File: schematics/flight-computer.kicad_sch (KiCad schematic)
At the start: 45 parts, among them J1 BATT, J2 SERIAL, J3 BLACKBOX, P1 SWD_TC, P2 GPS, P3 TLM, U1 MAX604, U10 MAX14787E, U11 MAX14787E, U12 NC7SZ04, U2 MAX604, U3 STM32F405RGT6, U9 CDCLVC1103PW, Y1 LFTCXO068373

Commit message: Complete revision 1 schematic
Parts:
- removed C1: 100n, Strix:C_0402, symbol Strix:C
- removed C2, C3, C5, C6: 10u, Strix:C_0402, symbol Strix:C
- removed C31: 10n, Strix:C_0402, symbol Strix:C
- removed C4: 1n, Strix:C_0402, symbol Strix:C
- removed J2: SERIAL, Strix:Molex_Nano-Fit_105314-1106, symbol Strix:Conn_01x06
- removed P1: SWD_TC, Strix:SWD_TC, symbol Strix:SWD_TC
- removed R1: 200k, Strix:R_0402, symbol Strix:R
- removed R10: 10, Strix:R_0402, symbol Strix:R
- removed R5: 120, Strix:R_0402, symbol Strix:R
- removed R8, R9: 510k, Strix:R_0402, symbol Strix:R
- removed U1, U2: MAX604, Strix:MAX604, symbol Strix:MAX604
- removed U10: MAX14787E, Strix:MAX14787E, symbol Strix:MAX14787E
- removed U12: NC7SZ04, cusf:SOT-23-5, symbol Strix:NC7SZ04
- removed U9: CDCLVC1103PW, Strix:CDCLVC1103PW, symbol Strix:CDCLVC1103PW
- removed Y1: LFTCXO068373, Strix:LFTCXO068373, symbol Strix:LFTCXO068373
- added D1, D10, D11, D2, D3, D4, D5, D6, D7, D8, D9: ESD_DIODE, cusf:D_0402, symbol Strix:ESD_DIODE
- added J1: SWD, symbol Strix:Conn_02x05
- added J3: CHG, symbol Strix:Conn_01x02
- added J4: USB MICRO B, symbol Strix:Conn_01x05
- R2: value 10 -> 10k; footprint Strix:R_0402 -> (none)
- R3: value 100k -> 10k; footprint Strix:R_0402 -> (none)
- renumbered C7 to C1, C16 to C10, C8 to C2, C9 to C3, C10 to C4, C11 to C5, C12 to C6, C13 to C7, C14 to C8, C15 to C9, D1 to D12, D2 to D13, J1 to J2, J3 to J5, P2 to P1, P3 to P2, R6 to R1, U3 to U1, U11 to U2
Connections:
- net RADIO_CLK is gone; now on net USB_FS_VBUS: R2.2
- net USART1_TX is gone; now on net USB_FS_VBUS: U1.42 (PA9)
- net 3v3: now also D4.2, J1.1 (Pin_1)
- net GND: now also R2.1, D10.1, D11.1, D4.1, D5.1, D6.1, D7.1, D8.1, D9.1, J1.3 (Pin_3), J1.5 (Pin_5), J1.9 (Pin_9), J4.5 (Pin_5); no longer J2.3 (Pin_3)
- net SWDIO: now also J1.2 (Pin_2)
- net UART4_RX+: now also D5.2
- net UART4_RX-: now also D7.2
- net UART4_TX+: now also D9.2
- net UART4_TX-: now also D11.2
- net USB_FS_VBUS: now reaches R3.1
- net USB_FS_D+: now reaches U1.44 (PA11)
- net USB_FS_D+: now also D10.2, J4.3 (Pin_3)
- net USB_FS_D-: now reaches U1.45 (PA12)
- net USB_FS_D-: now also D8.2, J4.2 (Pin_2)
- net CHG_SDN: now reaches U1.50 (PA15)
- net IMU_PR_CL: now reaches U1.58 (PB6)
- net IMU_PR_DA: now reaches U1.59 (PB7)
- net 1v8: no longer names the net of R3.2
- net 1v8: now also D6.2, J4.1 (Pin_1)
- net BATT_MON renamed PSU/BATT_MON
- net PSU/BATT_MON: now also D1.1
- net MCU_CLK: no longer names the net of U1.5 (PH0)
- net USART1_RX: no longer names the net of U1.43 (PA10)
- net VBATT renamed PSU/BATT+
- net PSU/BATT+: now also D3.1
- net ~{RST} renamed NRST
- net NRST: now also J1.10 (Pin_10)
- new net PSU/BATT-: D1.2, D3.2, J2.3 (Pin_3)
- new net PSU/CHG+: D2.1, J3.1 (Pin_1)
- new net PSU/CHG-: D2.2, J3.2 (Pin_2)
- new net SWCLK: J1.4 (Pin_4)
- new net SWO: J1.6 (Pin_6)
- no-connect marks 28 -> 24
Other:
- added sheet PSU (psu.kicad_sch)
- sheet Altimeter ports: added IMU_PR_CL, IMU_PR_DA; removed none
- sheet Radio ports: added none; removed RADIO_CLK
- note added: "8.9 - 22V DC Charger Input"
- note added: "Blackbox Serial (RS-485)"
- note added: "SWD"
- note added: "USB Serial Out"
- note removed: "1v8 Power (300mA Max)"
- note removed: "26MHz Oscillator"
- note removed: "3v3 Power (300mA Max)"
- note removed: "Clipped Sine -> LVCMOS"
- note removed: "Clock Buffer"
- note removed: "Clock Distribution"
- note removed: "Note: - 3-output IC used because 2-output version not in stock - RADIO_CLK line should be properly impedance matched (currently not) - Clock buffer requires ferrite bead (see datasheet) - Coupling cap on output of TCXO should be < 1n"
- note removed: "Programming Interface (SWD)"
- note removed: "Serial Out (RS-485)"
- note removed: "To Blackbox (RS-485)"
- note removed: "USART1 <-> RS-422"
- moved on the sheet: C1, C10, C2, C3, C4, C5, C6, C7, C8, C9, D12, D13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

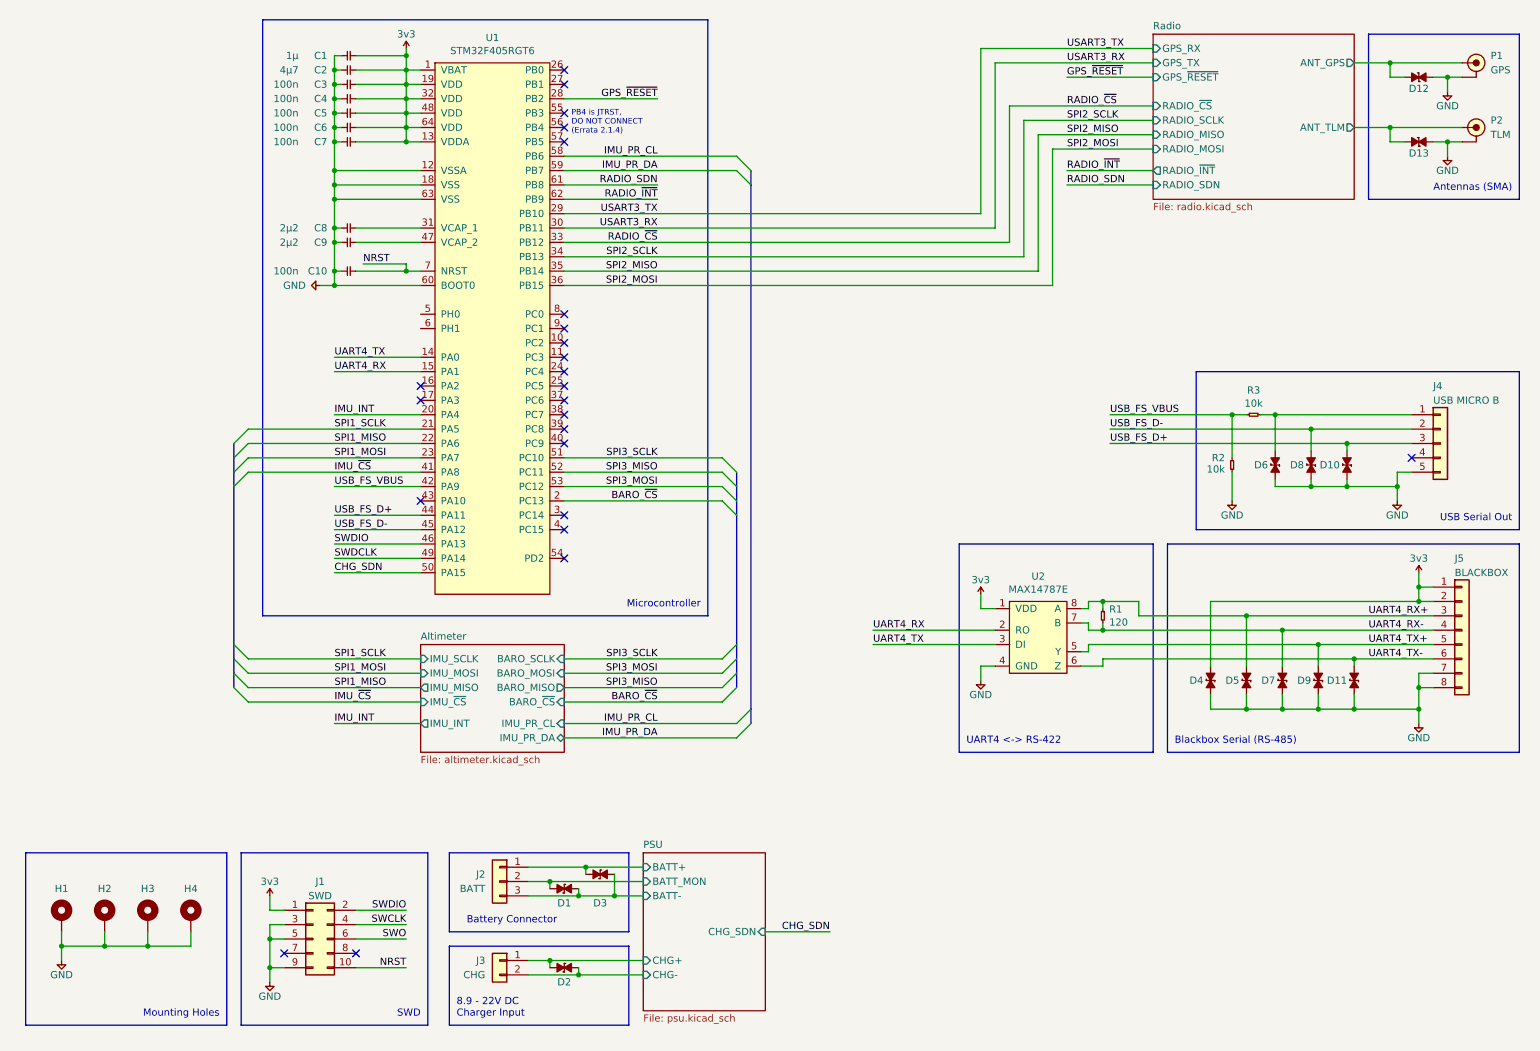
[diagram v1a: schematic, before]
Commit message: Add oscillators and clean up schematics
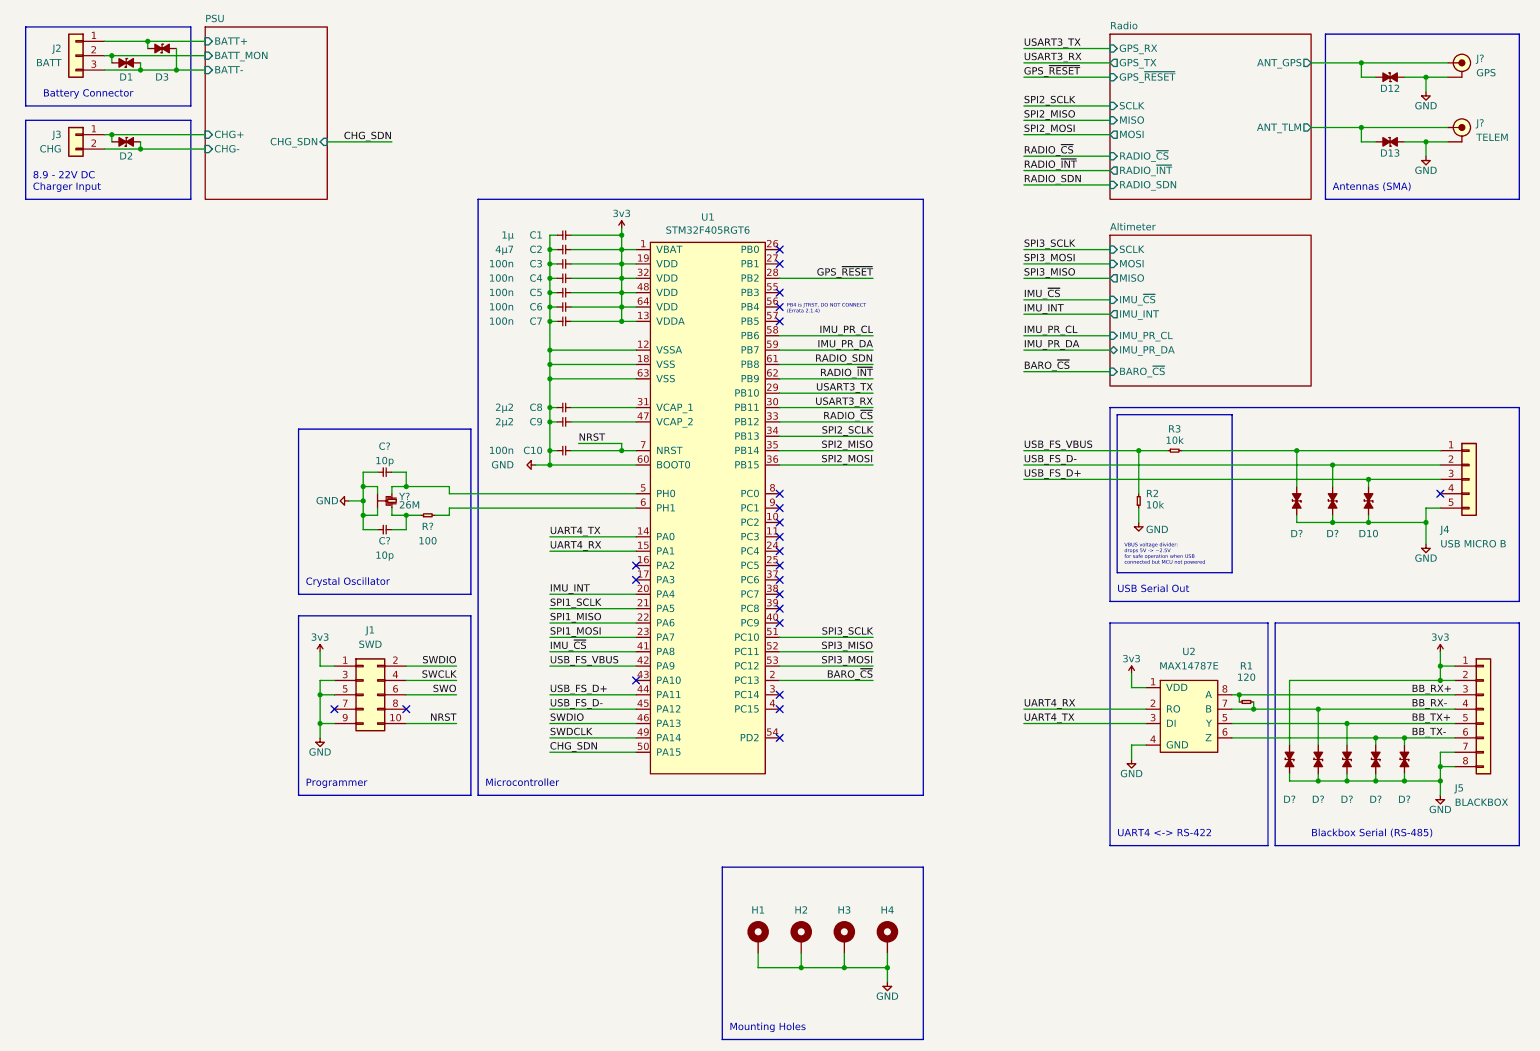
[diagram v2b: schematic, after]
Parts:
- removed D11, D4, D5, D6, D7, D8, D9: ESD_DIODE, cusf:D_0402, symbol Strix:ESD_DIODE
- removed P1: GPS, Strix:SMA-EDGE, symbol Strix:COAX
- removed P2: TLM, Strix:SMA-EDGE, symbol Strix:COAX
- added C? (x2): 10p, Strix:C_0402, symbol Strix:C
- added D? (x7): D_ESD, Strix:D_0402, symbol Strix:D_ESD
- added J?: GPS, Strix:SMA-EDGE, symbol Strix:Coax
- added J?: TELEM, Strix:SMA-EDGE, symbol Strix:Coax
- added R?: 100, Strix:R_0402, symbol Strix:R
- added Y?: 26M, symbol Strix:Xtal
- D1, D10, D2, D3: value ESD_DIODE -> D_ESD; footprint cusf:D_0402 -> Strix:D_0402; symbol Strix:ESD_DIODE -> Strix:D_ESD
- D12, D13: value ESD_DIODE -> D_ESD; symbol Strix:ESD_DIODE -> Strix:D_ESD
- R2, R3: footprint (none) -> Strix:R_0402
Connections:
- net 3v3: now also D?.2
- net GND: now also C?.1, C?.1, D?.1, D?.1, D?.1, D?.1, D?.1, D?.1, D?.1, J?.2 (GND), J?.2 (GND), Y?.2, Y?.4
- net Radio/ANT_GPS: now also J?.1 (RF)
- net Radio/ANT_TLM: now also J?.1 (RF)
- net USB_FS_D-: now also D?.2
- net at U1.5 (PH0): now also C?.2, Y?.1
- net at U1.6 (PH1): now also R?.2
- net at J4.1 (Pin_1), R3.2: now also D?.2
- net UART4_RX+ renamed BB_RX+
- net UART4_RX- renamed BB_RX-
- net BB_RX-: now also D?.2
- net UART4_TX+ renamed BB_TX+
- net BB_TX+: now also D?.2
- net UART4_TX- renamed BB_TX-
- net BB_TX-: now also D?.2, D?.2
- new net: C?.2, R?.1, Y?.3
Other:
- sheet Altimeter ports: added MISO, MOSI, SCLK; removed BARO_MISO, BARO_MOSI, BARO_SCLK, IMU_MISO, IMU_MOSI, IMU_SCLK
- sheet Radio ports: added MISO, MOSI, SCLK; removed RADIO_MISO, RADIO_MOSI, RADIO_SCLK
- note added: "Crystal Oscillator"
- note added: "Programmer"
- note added: "VBUS voltage divider: drops 5V -> ~2.5V for safe operation when USB connected but MCU not powered"
- note removed: "SWD"
- moved on the sheet: C1, C10, C2, C3, C4, C5, C6, C7, C8, C9, D1, D10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

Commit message: Fix broken symbol and footprint references
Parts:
- D1, D10, D12, D13, D2, D3, D? (x7): footprint Strix:D_0402 -> cusf:D_0402
- Y?: footprint (none) -> Strix:Xtal-20x16; Farnell (none) -> 2506952
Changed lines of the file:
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@@
       (effects (font (size 1.27 1.27)) (justify left) hide)
     )
-    (property "Footprint" "Strix:D_0402" (id 2) (at 256.54 31.75 0)
+    (property "Footprint" "cusf:D_0402" (id 2) (at 256.54 31.75 0)
       (effects (font (size 1.27 1.27)) (justify left) hide)
     )
@@
       (effects (font (size 1.27 1.27)) (justify left) hide)
     )
-    (property "Footprint" "Strix:D_0402" (id 2) (at 256.54 43.18 0)
+    (property "Footprint" "cusf:D_0402" (id 2) (at 256.54 43.18 0)
       (effects (font (size 1.27 1.27)) (justify left) hide)
     )
@@
       (effects (font (size 1.27 1.27)) (justify left) hide)
     )
-    (property "Footprint" "Strix:D_0402" (id 2) (at 250.19 148.59 0)
+    (property "Footprint" "cusf:D_0402" (id 2) (at 250.19 148.59 0)
       (effects (font (size 1.27 1.27)) (justify left) hide)
     )
@@
       (effects (font (size 1.27 1.27)) (justify left) hide)
     )
-    (property "Footprint" "Strix:D_0402" (id 2) (at 242.57 102.87 0)
+    (property "Footprint" "cusf:D_0402" (id 2) (at 242.57 102.87 0)
       (effects (font (size 1.27 1.27)) (justify left) hide)
     )
@@
       (effects (font (size 1.27 1.27)) (justify left) hide)
     )
-    (property "Footprint" "Strix:D_0402" (id 2) (at 255.27 148.59 0)
+    (property "Footprint" "cusf:D_0402" (id 2) (at 255.27 148.59 0)
       (effects (font (size 1.27 1.27)) (justify left) hide)
     )
@@
       (effects (font (size 1.27 1.27)) (justify left) hide)
     )
-    (property "Footprint" "Strix:D_0402" (id 2) (at 234.95 148.59 0)
+    (property "Footprint" "cusf:D_0402" (id 2) (at 234.95 148.59 0)
       (effects (font (size 1.27 1.27)) (justify left) hide)
     )
@@
       (effects (font (size 1.27 1.27)) (justify left top))
     )
-    (property "Footprint" "" (id 2) (at 75.692 101.6 0)
+    (property "Footprint" "Strix:Xtal-20x16" (id 2) (at 75.692 101.6 0)
       (effects (font (size 1.27 1.27)) hide)
     )
     (property "Datasheet" "" (id 3) (at 81.28 100.33 0)
+      (effects (font (size 1.27 1.27)) hide)
+    )
+    (property "Farnell" "2506952" (id 4) (at 81.28 100.33 90)
       (effects (font (size 1.27 1.27)) hide)
     )
@@
       (effects (font (size 1.27 1.27)) (justify left) hide)
     )
-    (property "Footprint" "Strix:D_0402" (id 2) (at 33.02 19.05 0)
+    (property "Footprint" "cusf:D_0402" (id 2) (at 33.02 19.05 0)
       (effects (font (size 1.27 1.27)) (justify left) hide)
     )
@@
       (effects (font (size 1.27 1.27)) (justify left) hide)
     )
-    (property "Footprint" "Strix:D_0402" (id 2) (at 39.37 16.51 0)
+    (property "Footprint" "cusf:D_0402" (id 2) (at 39.37 16.51 0)
       (effects (font (size 1.27 1.27)) (justify left) hide)
     )
@@
       (effects (font (size 1.27 1.27)) (justify left) hide)
     )
-    (property "Footprint" "Strix:D_0402" (id 2) (at 240.03 148.59 0)
+    (property "Footprint" "cusf:D_0402" (id 2) (at 240.03 148.59 0)
       (effects (font (size 1.27 1.27)) (justify left) hide)
     )
@@
       (effects (font (size 1.27 1.27)) (justify left) hide)
     )
-    (property "Footprint" "Strix:D_0402" (id 2) (at 248.92 102.87 0)
+    (property "Footprint" "cusf:D_0402" (id 2) (at 248.92 102.87 0)
       (effects (font (size 1.27 1.27)) (justify left) hide)
     )
@@
       (effects (font (size 1.27 1.27)) (justify left) hide)
     )
-    (property "Footprint" "Strix:D_0402" (id 2) (at 245.11 148.59 0)
+    (property "Footprint" "cusf:D_0402" (id 2) (at 245.11 148.59 0)
       (effects (font (size 1.27 1.27)) (justify left) hide)
     )
@@
       (effects (font (size 1.27 1.27)) (justify left) hide)
     )
-    (property "Footprint" "Strix:D_0402" (id 2) (at 33.02 33.02 0)
+    (property "Footprint" "cusf:D_0402" (id 2) (at 33.02 33.02 0)
       (effects (font (size 1.27 1.27)) (justify left) hide)
     )
@@
       (effects (font (size 1.27 1.27)) (justify left) hide)
     )
-    (property "Footprint" "Strix:D_0402" (id 2) (at 236.22 102.87 0)
+    (property "Footprint" "cusf:D_0402" (id 2) (at 236.22 102.87 0)
       (effects (font (size 1.27 1.27)) (justify left) hide)
     )
@@
     )
     (path "/9f5b92df-a9fc-40a8-958b-14377f29c85a"
-      (reference "D1") (unit 1) (value "D_ESD") (footprint "Strix:D_0402")
+      (reference "D1") (unit 1) (value "D_ESD") (footprint "cusf:D_0402")
     )
     (path "/e26e50c4-cf70-4f87-928a-0e6d36a91c09"
-      (reference "D2") (unit 1) (value "D_ESD") (footprint "Strix:D_0402")
+      (reference "D2") (unit 1) (value "D_ESD") (footprint "cusf:D_0402")
     )
     (path "/c3b69905-b979-4ca9-8e95-d758dcfb4921"
-      (reference "D3") (unit 1) (value "D_ESD") (footprint "Strix:D_0402")
+      (reference "D3") (unit 1) (value "D_ESD") (footprint "cusf:D_0402")
     )
     (path "/d36269cf-fe8c-4740-ac3a-02fa7488e4e2"
-      (reference "D10") (unit 1) (value "D_ESD") (footprint "Strix:D_0402")
+      (reference "D10") (unit 1) (value "D_ESD") (footprint "cusf:D_0402")
     )
     (path "/00000000-0000-0000-0000-000060d1b9af"
-      (reference "D12") (unit 1) (value "D_ESD") (footprint "Strix:D_0402")
+      (reference "D12") (unit 1) (value "D_ESD") (footprint "cusf:D_0402")
     )
     (path "/00000000-0000-0000-0000-000060d652b8"
-      (reference "D13") (unit 1) (value "D_ESD") (footprint "Strix:D_0402")
+      (reference "D13") (unit 1) (value "D_ESD") (footprint "cusf:D_0402")
     )
     (path "/0560d9e6-7a86-479d-84fc-0ec915d62cea/6d89a26b-fadc-4d42-8ad7-831c9a1bef6d"
@@
     )
     (path "/13916f25-a64a-411b-bcf0-66cd269ab1d5"
-      (reference "D?") (unit 1) (value "D_ESD") (footprint "Strix:D_0402")
+      (reference "D?") (unit 1) (value "D_ESD") (footprint "cusf:D_0402")
     )
     (path "/2ac89f34-2885-441c-8a07-6d3539cc8270"
-      (reference "D?") (unit 1) (value "D_ESD") (footprint "Strix:D_0402")
+      (reference "D?") (unit 1) (value "D_ESD") (footprint "cusf:D_0402")
     )
     (path "/696527dd-3c5b-4dc5-bb82-f499fd6dca2d"
-      (reference "D?") (unit 1) (value "D_ESD") (footprint "Strix:D_0402")
+      (reference "D?") (unit 1) (value "D_ESD") (footprint "cusf:D_0402")
     )
     (path "/897d8e03-cc99-497d-94e1-07c9a72484e0"
-      (reference "D?") (unit 1) (value "D_ESD") (footprint "Strix:D_0402")
+      (reference "D?") (unit 1) (value "D_ESD") (footprint "cusf:D_0402")
     )
     (path "/c53f9a1a-813c-4324-b221-cedf75304ce7"
-      (reference "D?") (unit 1) (value "D_ESD") (footprint "Strix:D_0402")
+      (reference "D?") (unit 1) (value "D_ESD") (footprint "cusf:D_0402")
     )
     (path "/de5a4ede-b270-453a-b488-596030c813d8"
-      (reference "D?") (unit 1) (value "D_ESD") (footprint "Strix:D_0402")
+      (reference "D?") (unit 1) (value "D_ESD") (footprint "cusf:D_0402")
     )
     (path "/ed524139-d90d-40e9-94d4-80bbe1243464"
-      (reference "D?") (unit 1) (value "D_ESD") (footprint "Strix:D_0402")
+      (reference "D?") (unit 1) (value "D_ESD") (footprint "cusf:D_0402")
     )
     (path "/00000000-0000-0000-0000-000061342567"
@@
     )
     (path "/0560d9e6-7a86-479d-84fc-0ec915d62cea/2bd88b42-a583-4824-8baf-4ecac716152a"
-      (reference "Q1") (unit 1) (value "Si9933CDY") (footprint "Battery:SOIC-8_3.9x4.9mm_P1.27mm")
+      (reference "Q1") (unit 1) (value "Si9933CDY") (footprint "Strix:Si9933CDY")
     )
     (path "/0560d9e6-7a86-479d-84fc-0ec915d62cea/eb3b75c6-f775-48c1-aa10-2016bd53ab26"
-      (reference "Q1") (unit 2) (value "Si9933CDY") (footprint "Battery:SOIC-8_3.9x4.9mm_P1.27mm")
+      (reference "Q1") (unit 2) (value "Si9933CDY") (footprint "Strix:Si9933CDY")
     )
     (path "/0560d9e6-7a86-479d-84fc-0ec915d62cea/b4cc3f2a-f2be-4f94-9ec8-4eec9cf55a9d"
-      (reference "Q2") (unit 1) (value "BSS138") (footprint "Package_TO_SOT_SMD:SOT-23")
+      (reference "Q2") (unit 1) (value "BSS138") (footprint "Strix:BSS138")
     )
     (path "/00000000-0000-0000-0000-0000618d7b1a"
@@
       (reference "U8") (unit 1) (value "MAX-M8Q") (footprint "Strix:MAX-M8Q")
     )
-    (path "/0560d9e6-7a86-479d-84fc-0ec915d62cea/c9b07493-f9b4-4c69-8a3c-7a5de1827736"
-      (reference "U9") (unit 1) (value "BQ29200") (footprint "Battery:BQ2920X")
-    )
     (path "/0560d9e6-7a86-479d-84fc-0ec915d62cea/1eb42abd-1deb-463e-b751-41637bf1529b"
-      (reference "U10") (unit 1) (value "LTC4002ES8") (footprint "Battery:SO-8_3.9x4.9mm_P1.27mm")
+      (reference "U10") (unit 1) (value "LTC4002-ES8") (footprint "Strix:LTC4002-ES8")
     )
     (path "/0560d9e6-7a86-479d-84fc-0ec915d62cea/c8363d47-9959-4a99-ba05-3ea13938c61f"
@@
       (reference "U12") (unit 1) (value "MAX604") (footprint "Strix:MAX604")
     )
+    (path "/0560d9e6-7a86-479d-84fc-0ec915d62cea/efa65d84-4d33-4d24-8ecd-912f1b43323c"
+      (reference "U?") (unit 1) (value "BQ29200") (footprint "Strix:BQ29200")
+    )
     (path "/96d64ec3-74dd-45f3-9f77-b1b10a62a585"
-      (reference "Y?") (unit 1) (value "26M") (footprint "")
+      (reference "Y?") (unit 1) (value "26M") (footprint "Strix:Xtal-20x16")
     )
     (path "/00000000-0000-0000-0000-0000611291b2/f4f237e8-d7a6-465e-996a-94072554fcb5"
